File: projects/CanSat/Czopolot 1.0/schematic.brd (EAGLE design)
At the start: 35.6 x 50.8 mm, 16 parts

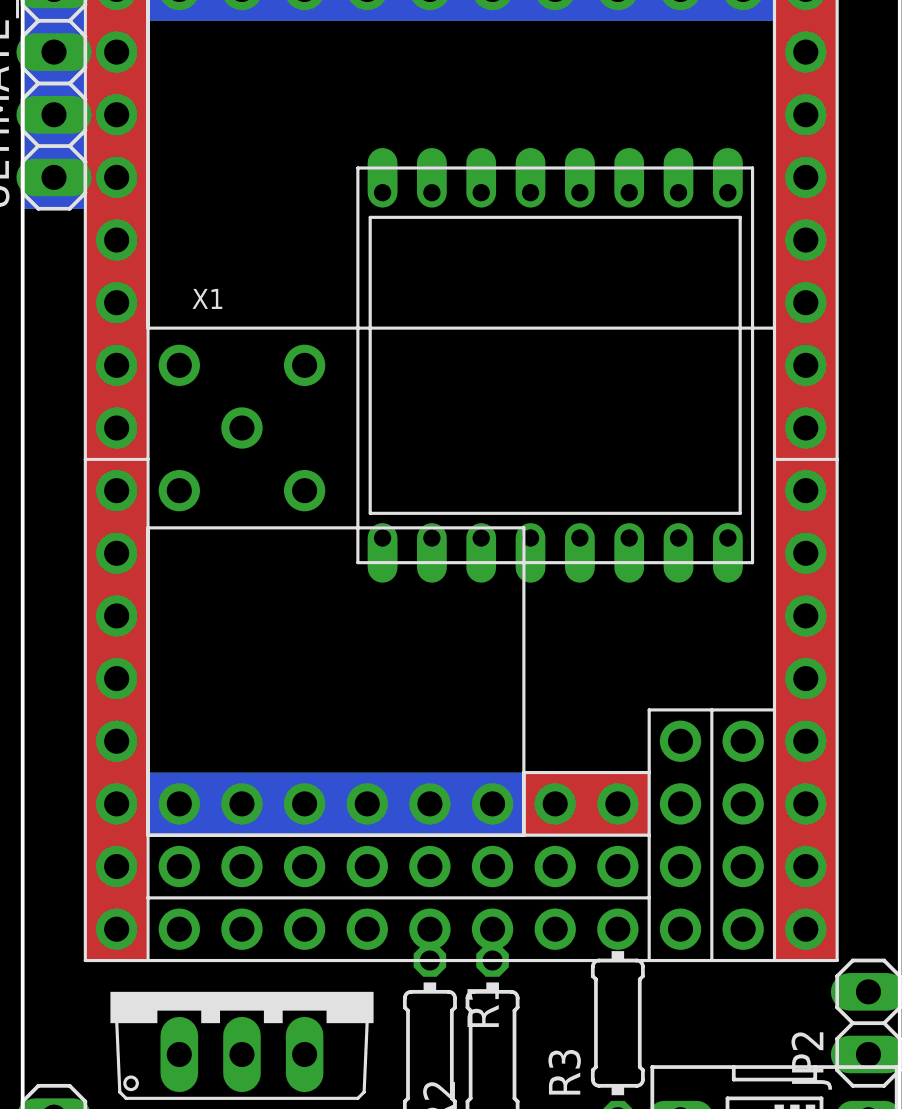
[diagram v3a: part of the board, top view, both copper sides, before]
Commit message: Switched SX1280
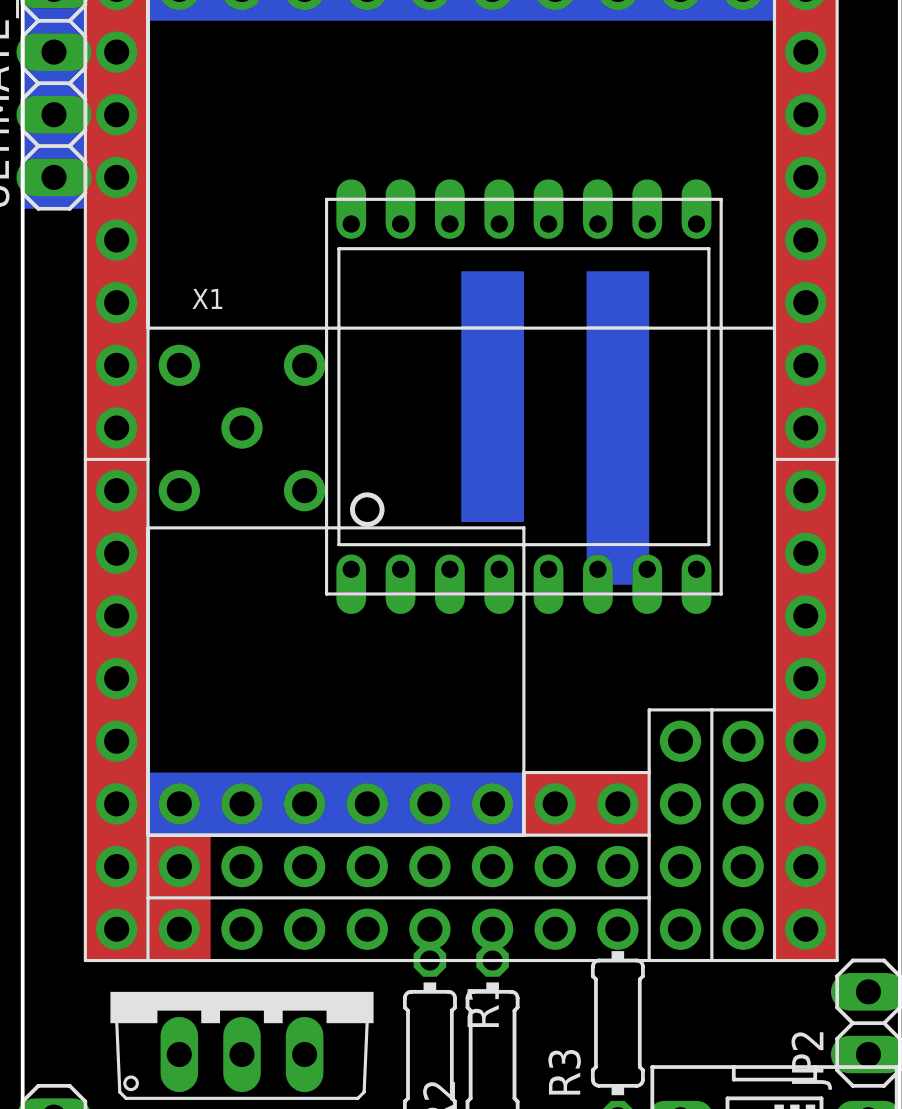
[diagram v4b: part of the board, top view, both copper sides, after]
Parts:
- removed U$2: SX1280, SobieskiSat2:MODULE_SX1280
- added U$6: SX1280_2.4GHZ, SobieskiSat2:MODULE_SX1280_THT
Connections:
- new net BUSY: U$1.X3, U$6.BUSY
- new net NRESET: U$1.X2, U$6.NRESET
- net DIO1: now also U$1.X4; no longer U$1.X3, U$2.DIO1
- net GND: now also U$6.GND@3, U$6.GND@4, U$6.GND@5; no longer U$2.GND@1, U$2.GND@2, U$2.GND@3, U$2.GND@4, U$2.GND@5
- net N$1: now also U$1.X5, U$6.NSS; no longer U$1.Y9, U$2.MOSI
- net N$14: now also R3.2; no longer R3.1, U$5.3
- net N$2: now also U$1.X6, U$6.SCK; no longer U$1.X8, U$2.MISO
- net N$3: now also U$1.X8, U$6.MOSI; no longer U$1.X7, U$2.SCK
- net N$4: now also U$1.X7, U$6.MISO; no longer U$1.X6, U$2.NSS
- net N$5: now also U$6.ANT, X1.ANTENNA; no longer U$1.X5, U$2.BUSY
- net N$6: now also U$6.DIO1; no longer U$1.X4, U$2.NRESET
- net N$7: now also R3.1, U$5.3; no longer U$2.ANT, X1.ANTENNA
- net VCC: now also U$6.VCC; no longer U$2.VCC
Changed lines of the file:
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@@
 <wire x1="38.1" y1="-50.8" x2="2.54" y2="-50.8" width="0.1524" layer="20"/>
 <wire x1="2.54" y1="-50.8" x2="2.54" y2="0" width="0.1524" layer="20"/>
+<rectangle x1="7.62" y1="-40.64" x2="10.16" y2="-35.56" layer="1"/>
+<rectangle x1="25.4" y1="-25.4" x2="27.94" y2="-12.7" layer="16"/>
+<rectangle x1="20.32" y1="-22.86" x2="22.86" y2="-12.7" layer="16"/>
 </plain>
 <attributes>
@@
 <attribute name="VALUE" x="6.985" y="-10.16" size="1.27" layer="27" rot="R90"/>
 </element>
-<element name="U$2" library="SobieskiSat2" package="MODULE_SX1280" value="SX1280" x="24.13" y="-16.51" smashed="yes" rot="R270"/>
 <element name="X1" library="SobieskiSat2" package="SMA_DIP" package3d_urn="urn:adsk.eagle:package:6240946/1" value="" x="11.43" y="-19.05" smashed="yes">
 <attribute name="NAME" x="9.398" y="-14.224" size="0.8128" layer="25" ratio="18"/>
@@
 <attribute name="VALUE" x="61.595" y="-30.2006" size="1.27" layer="27" ratio="10" rot="R90"/>
 </element>
+<element name="U$6" library="SobieskiSat2" package="MODULE_SX1280_THT" value="SX1280_2.4GHZ" x="22.86" y="-17.78" smashed="yes" rot="R90"/>
 </elements>
 <signals>
@@
 <signal name="GND" airwireshidden="yes">
 <contactref element="ULTIMATE_GPS" pad="2"/>
-<contactref element="U$2" pad="GND@1"/>
-<contactref element="U$2" pad="GND@2"/>
-<contactref element="U$2" pad="GND@3"/>
-<contactref element="U$2" pad="GND@4"/>
-<contactref element="U$2" pad="GND@5"/>
 <contactref element="U$4" pad="GND"/>
 <contactref element="U$3" pad="GND"/>
 <contactref element="U$5" pad="1"/>
 <contactref element="U$5" pad="2"/>
-<wire x1="25.13" y1="-9.51" x2="29.21" y2="-1.271" width="0" layer="19" extent="1-1"/>
-<wire x1="27.13" y1="-23.51" x2="25.13" y2="-9.51" width="0" layer="19" extent="1-1"/>
-<wire x1="23.13" y1="-23.51" x2="27.13" y2="-23.51" width="0" layer="19" extent="1-1"/>
-<wire x1="21.13" y1="-23.51" x2="23.13" y2="-23.51" width="0" layer="19" extent="1-1"/>
-<wire x1="19.13" y1="-23.51" x2="21.13" y2="-23.51" width="0" layer="19" extent="1-1"/>
-<wire x1="11.43" y1="-34.289" x2="19.13" y2="-23.51" width="0" layer="19" extent="1-1"/>
-<wire x1="3.81" y1="-6.35" x2="25.13" y2="-9.51" width="0" layer="19" extent="1-1"/>
-<wire x1="36.83" y1="-46.99" x2="27.13" y2="-23.51" width="0" layer="19" extent="1-1"/>
+<contactref element="U$6" pad="GND@3"/>
+<contactref element="U$6" pad="GND@4"/>
+<contactref element="U$6" pad="GND@5"/>
+<wire x1="27.86" y1="-10.78" x2="29.21" y2="-1.271" width="0" layer="19" extent="1-1"/>
+<wire x1="25.86" y1="-10.78" x2="27.86" y2="-10.78" width="0" layer="19" extent="1-1"/>
+<wire x1="21.86" y1="-24.78" x2="25.86" y2="-10.78" width="0" layer="19" extent="1-1"/>
+<wire x1="11.43" y1="-34.289" x2="21.86" y2="-24.78" width="0" layer="19" extent="1-1"/>
+<wire x1="3.81" y1="-6.35" x2="25.86" y2="-10.78" width="0" layer="19" extent="1-1"/>
+<wire x1="36.83" y1="-46.99" x2="21.86" y2="-24.78" width="0" layer="19" extent="1-1"/>
 <wire x1="36.83" y1="-49.53" x2="36.83" y2="-46.99" width="0" layer="19" extent="1-1"/>
-</signal>
-<signal name="N$1">
-<contactref element="U$2" pad="MOSI"/>
-<contactref element="U$1" pad="Y9"/>
-<wire x1="21.13" y1="-9.51" x2="34.29" y2="-19.05" width="0" layer="19" extent="1-1"/>
-</signal>
-<signal name="N$2">
-<contactref element="U$2" pad="MISO"/>
-<contactref element="U$1" pad="X8"/>
-<wire x1="34.29" y1="-21.59" x2="23.13" y2="-9.51" width="0" layer="19" extent="1-1"/>
-</signal>
-<signal name="N$3">
-<contactref element="U$2" pad="SCK"/>
-<contactref element="U$1" pad="X7"/>
-<wire x1="34.29" y1="-24.13" x2="19.13" y2="-9.51" width="0" layer="19" extent="1-1"/>
-</signal>
-<signal name="N$4">
-<contactref element="U$2" pad="NSS"/>
-<contactref element="U$1" pad="X6"/>
-<wire x1="34.29" y1="-26.67" x2="17.13" y2="-9.51" width="0" layer="19" extent="1-1"/>
-</signal>
-<signal name="N$5">
-<contactref element="U$2" pad="BUSY"/>
-<contactref element="U$1" pad="X5"/>
-<wire x1="34.29" y1="-29.21" x2="29.13" y2="-23.51" width="0" layer="19" extent="1-1"/>
-</signal>
-<signal name="N$6">
-<contactref element="U$2" pad="NRESET"/>
-<contactref element="U$1" pad="X4"/>
-<wire x1="25.13" y1="-23.51" x2="34.29" y2="-31.75" width="0" layer="19" extent="1-1"/>
 </signal>
 <signal name="GND1">
@@
 <contactref element="X1" pad="GND4"/>
 </signal>
-<signal name="N$7">
-<contactref element="U$2" pad="ANT"/>
-<contactref element="X1" pad="ANTENNA"/>
-<wire x1="11.43" y1="-19.05" x2="17.13" y2="-23.51" width="0" layer="19" extent="1-1"/>
-</signal>
 <signal name="VCC" airwireshidden="yes">
-<contactref element="U$2" pad="VCC"/>
 <contactref element="U$3" pad="VCC"/>
 <contactref element="U$4" pad="VCC"/>
 <contactref element="U$1" pad="3V3-1"/>
 <contactref element="U$1" pad="3V3"/>
-<wire x1="34.29" y1="-3.81" x2="31.75" y2="-1.271" width="0" layer="19" extent="1-1"/>
-<wire x1="27.13" y1="-9.51" x2="34.29" y2="-3.81" width="0" layer="19" extent="1-1"/>
-<wire x1="8.89" y1="-34.289" x2="27.13" y2="-9.51" width="0" layer="19" extent="1-1"/>
-<wire x1="6.35" y1="-36.83" x2="8.89" y2="-34.289" width="0" layer="19" extent="1-1"/>
+<contactref element="U$6" pad="VCC"/>
+<wire x1="6.35" y1="-36.83" x2="19.86" y2="-24.78" width="0" layer="19" extent="1-1"/>
+<wire x1="8.89" y1="-34.289" x2="6.35" y2="-36.83" width="0" layer="19" extent="1-1"/>
+<wire x1="34.29" y1="-3.81" x2="8.89" y2="-34.289" width="0" layer="19" extent="1-1"/>
+<wire x1="31.75" y1="-1.271" x2="34.29" y2="-3.81" width="0" layer="19" extent="1-1"/>
 </signal>
 <signal name="N$8">
@@
 </signal>
 <signal name="BAT-">
-</signal>
-<signal name="DIO1">
-<contactref element="U$2" pad="DIO1"/>
-<contactref element="U$1" pad="X3"/>
-<wire x1="34.29" y1="-34.29" x2="31.13" y2="-23.51" width="0" layer="19" extent="1-1"/>
 </signal>
 <signal name="V+" airwireshidden="yes">
@@
 </signal>
 <signal name="N$14">
+<contactref element="U$1" pad="X17"/>
+<contactref element="R3" pad="2"/>
+<wire x1="26.67" y1="-39.37" x2="8.89" y2="-39.37" width="0" layer="19" extent="1-1"/>
+</signal>
+<signal name="N$1">
+<contactref element="U$6" pad="NSS"/>
+<contactref element="U$1" pad="X5"/>
+<wire x1="34.29" y1="-29.21" x2="29.86" y2="-24.78" width="0" layer="19" extent="1-1"/>
+</signal>
+<signal name="N$2">
+<contactref element="U$6" pad="SCK"/>
+<contactref element="U$1" pad="X6"/>
+<wire x1="34.29" y1="-26.67" x2="27.86" y2="-24.78" width="0" layer="19" extent="1-1"/>
+</signal>
+<signal name="N$3">
+<contactref element="U$6" pad="MOSI"/>
+<contactref element="U$1" pad="X8"/>
+<wire x1="34.29" y1="-21.59" x2="25.86" y2="-24.78" width="0" layer="19" extent="1-1"/>
+</signal>
+<signal name="N$4">
+<contactref element="U$6" pad="MISO"/>
+<contactref element="U$1" pad="X7"/>
+<wire x1="34.29" y1="-24.13" x2="23.86" y2="-24.78" width="0" layer="19" extent="1-1"/>
+</signal>
+<signal name="N$5">
+<contactref element="U$6" pad="ANT"/>
+<contactref element="X1" pad="ANTENNA"/>
+<wire x1="11.43" y1="-19.05" x2="29.86" y2="-10.78" width="0" layer="19" extent="1-1"/>
+</signal>
+<signal name="N$6">
+<contactref element="U$6" pad="DIO1"/>
+</signal>
+<signal name="BUSY">
+<contactref element="U$6" pad="BUSY"/>
+<contactref element="U$1" pad="X3"/>
+<wire x1="34.29" y1="-34.29" x2="17.86" y2="-10.78" width="0" layer="19" extent="1-1"/>
+</signal>
+<signal name="DIO1">
+<contactref element="U$1" pad="X4"/>
+</signal>
+<signal name="NRESET">
+<contactref element="U$1" pad="X2"/>
+<contactref element="U$6" pad="NRESET"/>
+<wire x1="34.29" y1="-36.83" x2="21.86" y2="-10.78" width="0" layer="19" extent="1-1"/>
+</signal>
+<signal name="N$7">
 <contactref element="U$5" pad="3"/>
-<contactref element="U$1" pad="X17"/>
 <contactref element="R3" pad="1"/>
-<wire x1="26.67" y1="-46.99" x2="8.89" y2="-39.37" width="0" layer="19" extent="1-1"/>
 <wire x1="29.21" y1="-46.99" x2="26.67" y2="-46.99" width="0" layer="19" extent="1-1"/>
 </signal>
